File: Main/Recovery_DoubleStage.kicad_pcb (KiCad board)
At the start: 4 copper layers, 100.6 x 76.7 mm, 68 parts, among them IC1 ATMEGA2560-16AU, IC2 AP2210N-3.3TRG1, IC3 MMC5983MA, IC4 NEO-6M-0, IC5 BMP388, IC6 MPU-6050, J1 ICSP, J2 Conn_02x10_Counter_Clockwise, J3 Conn_Coaxial, J4 Conn_Coaxial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

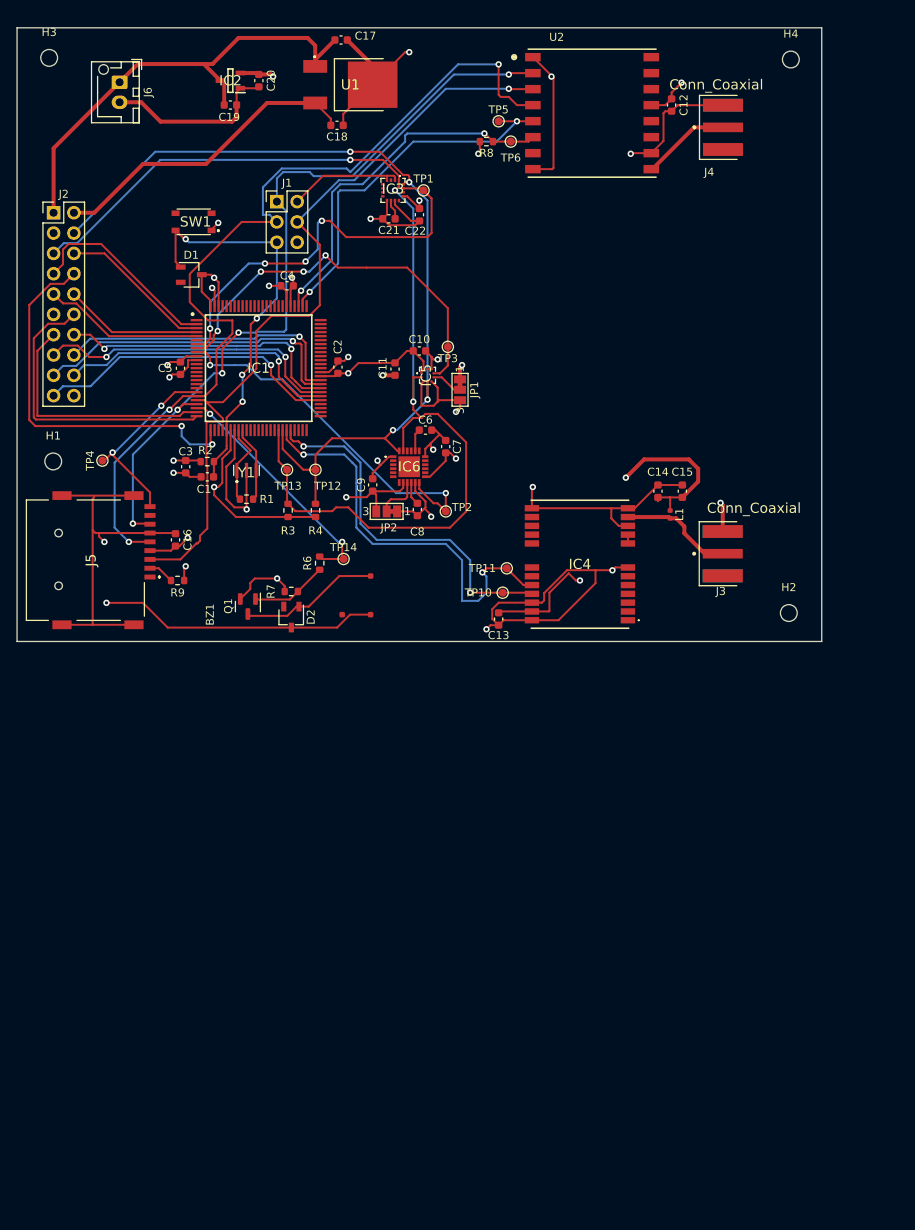
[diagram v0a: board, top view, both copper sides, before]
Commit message: added relative paths
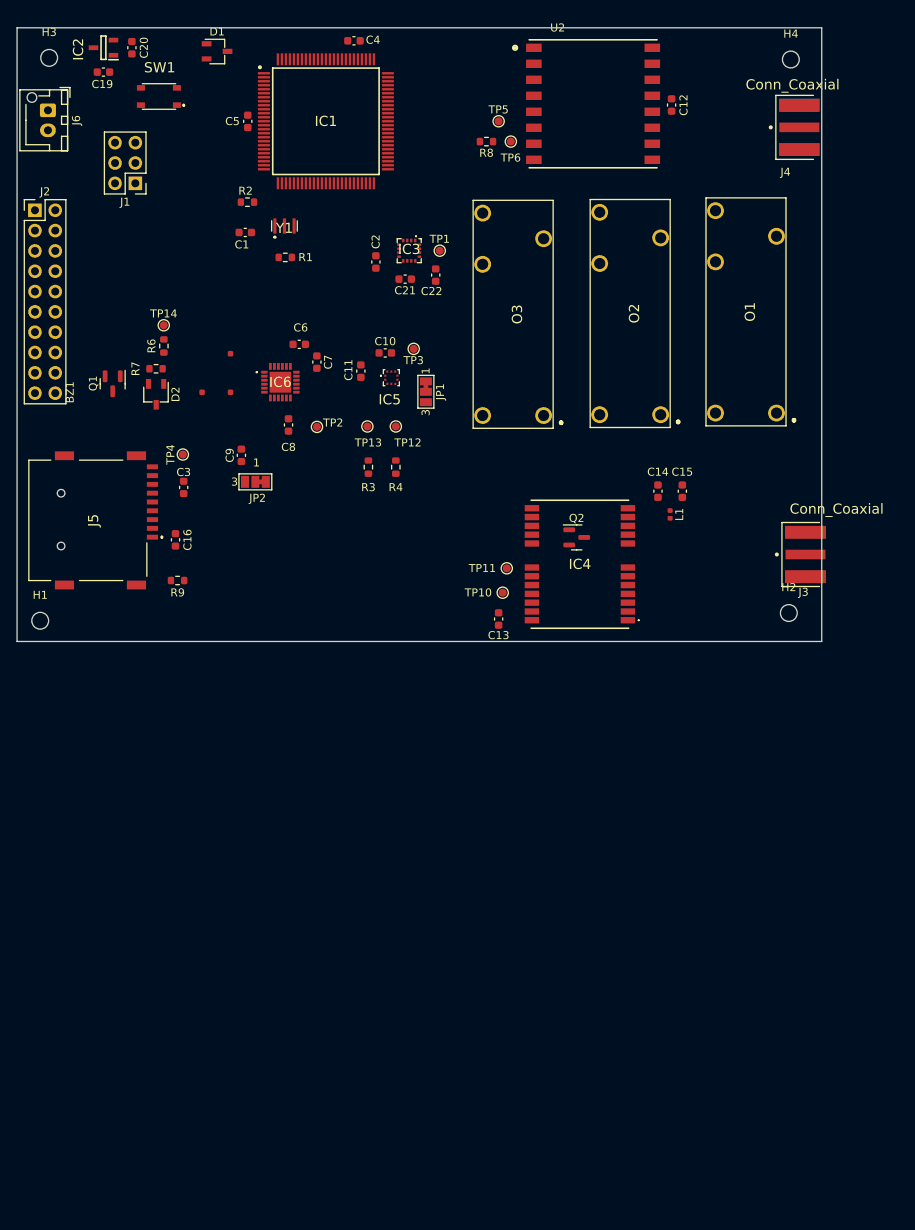
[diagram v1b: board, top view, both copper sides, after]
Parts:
- removed C17, C18: 10u, Capacitor_SMD:C_0603_1608Metric
- removed U1: NCP5501DT50RKG, Footprint:NCP5501DT50RKG
- added O1: G6RL-1-DC3, Footprint:G6RL1DC5, F.Cu at (107.4, 61.4)
- added O2: G6RL-1-DC3, Footprint:G6RL1DC5, F.Cu at (92.9, 61.6)
- added O3: G6RL-1-DC3, Footprint:G6RL1DC5, F.Cu at (78.3, 61.7)
- added Q2: BSS138, Package_TO_SOT_SMD:SOT-23, F.Cu at (82.4, 76.9)
- moved TP14 36.9 mm to (30.8, 50.4)
- moved R6 33.4 mm to (30.8, 53.0)
- moved BZ1 32.8 mm to (39.4, 58.8)
- moved R2 32.8 mm to (41.2, 35.0)
- moved Q1 32.6 mm to (24.4, 57.7)
- moved D2 32.6 mm to (29.8, 59.0)
- moved R7 32.6 mm to (29.8, 55.8)
- moved IC1 32.0 mm to (51.1, 24.9)
- moved C5 32.0 mm to (41.3, 24.9)
- moved C4 31.7 mm to (54.6, 14.8)
- moved C1 30.9 mm to (41.0, 38.8)
- moved Y1 30.9 mm to (45.9, 38.4)
- moved R1 30.6 mm to (46.0, 41.9)
- moved D1 28.1 mm to (37.5, 16.2)
- moved H1 20.0 mm to (15.3, 87.3)
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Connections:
- J2 pad 14: /IGNITION -> unconnected-(J2-Pad14)
- J2 pad 15: /ID3 -> unconnected-(J2-Pad15)
- J2 pad 16: /Relay_2 -> unconnected-(J2-Pad16)
- J2 pad 17: /Relay_1 -> unconnected-(J2-Pad17)
- J2 pad 18: /ID2 -> unconnected-(J2-Pad18)
- J2 pad 19: /ID1 -> unconnected-(J2-Pad19)
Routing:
- net GND: track 288.5 -> 0.00 mm, vias 23 -> 0
- net +3V3: track 188.2 -> 0.00 mm, vias 17 -> 0
- net /SCL: track 140.6 -> 0.00 mm, vias 3 -> 0
- net +5V: track 125.7 -> 0.00 mm, vias 1 -> 0
- net /SCK: track 112.7 -> 0.00 mm, vias 3 -> 0
- net /SDA: track 112.4 -> 0.00 mm, vias 4 -> 0
- net /MOSI: track 99.1 -> 0.00 mm, vias 1 -> 0
- net /MISO: track 98.2 -> 0.00 mm, vias 5 -> 0
- net +BATT: track 58.5 -> 0.00 mm
- net /RX1: track 52.4 -> 0.00 mm, vias 2 -> 0
- net /microcontroller/RESET: track 50.8 -> 0.00 mm, vias 4 -> 0
- net /BMP_INT: track 49.9 -> 0.00 mm, vias 4 -> 0
- net /MMC_INT: track 49.8 -> 0.00 mm, vias 4 -> 0
- net /OPT1: track 48.3 -> 0.00 mm, vias 2 -> 0
- net /MPU_INT: track 46.6 -> 0.00 mm, vias 2 -> 0
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- removed copper zone on In2.Cu, net +3V3
- removed copper zone on In1.Cu, net GND

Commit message: reviewed design. starting routing
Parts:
- removed C19, C20: 10u, Capacitor_SMD:C_0603_1608Metric
- removed IC2: AP2210N-3.3TRG1, Footprint:SOT95P280X145-3N
- added C17: 4.7u, Capacitor_SMD:C_0603_1608Metric, F.Cu at (21.1, 16.9)
- added C18: 10u, Capacitor_SMD:C_0603_1608Metric, F.Cu at (25.1, 20.2)
- added D3: D, Package_TO_SOT_SMD:TSOT-23, F.Cu at (62.5, 143.6)
- added D4: D, Package_TO_SOT_SMD:TSOT-23, F.Cu at (57.1, 143.6)
- added D5: D, Package_TO_SOT_SMD:TSOT-23, F.Cu at (67.9, 143.6)
- added IC7: PS2801C-4-F3-A, Footprint:SOIC127P700X230-16N, F.Cu at (41.2, 147.4)
- added J7: Screw_Terminal_01x06, TerminalBlock:TerminalBlock_bornier-6_P5.08mm, F.Cu at (39.7, 122.7)
- added J8: JSTXH-1x02, Connector_JST:JST_XH_B2B-XH-AM_1x02_P2.50mm_Vertical, F.Cu at (66.4, 131.1)
- added L2: 1uH, Inductor_SMD:L_0805_2012Metric, F.Cu at (27.9, 17.2)
- added Q3: BSS138, Package_TO_SOT_SMD:SOT-23, F.Cu at (73.0, 142.3)
- added Q4: BSS138, Package_TO_SOT_SMD:SOT-23, F.Cu at (77.9, 142.3)
- added R10: 100k, Resistor_SMD:R_0603_1608Metric, F.Cu at (60.4, 149.6)
- added R11: 100k, Resistor_SMD:R_0603_1608Metric, F.Cu at (48.0, 152.8)
- added R12: 1k, Resistor_SMD:R_0603_1608Metric, F.Cu at (64.0, 152.1)
- added R13: 1k, Resistor_SMD:R_0603_1608Metric, F.Cu at (56.0, 152.8)
- added R14: 1k, Resistor_SMD:R_0603_1608Metric, F.Cu at (64.5, 149.6)
- added R15: 100, Resistor_SMD:R_0603_1608Metric, F.Cu at (52.0, 152.8)
- added R16: 10k, Resistor_SMD:R_0603_1608Metric, F.Cu at (79.4, 133.6)
- added R17: 100, Resistor_SMD:R_0603_1608Metric, F.Cu at (68.0, 152.1)
- added R18: 10k, Resistor_SMD:R_0603_1608Metric, F.Cu at (68.5, 149.6)
- added R19: 100, Resistor_SMD:R_0603_1608Metric, F.Cu at (60.0, 152.1)
- added R20: 100, Resistor_SMD:R_0603_1608Metric, F.Cu at (56.4, 149.6)
- added R21: 100, Resistor_SMD:R_0603_1608Metric, F.Cu at (64.0, 147.1)
- added R22: 100, Resistor_SMD:R_0603_1608Metric, F.Cu at (72.0, 147.1)
- added R23: 10k, Resistor_SMD:R_0603_1608Metric, F.Cu at (60.0, 147.1)
- added R24: 330k, Resistor_SMD:R_0603_1608Metric, F.Cu at (107.9, 125.7)
- added R25: 100k, Resistor_SMD:R_0603_1608Metric, F.Cu at (70.7, 25.1)
- added R26: 330, Resistor_SMD:R_0603_1608Metric, F.Cu at (116.7, 119.4)
- added R27: 330, Resistor_SMD:R_0603_1608Metric, F.Cu at (111.9, 125.7)
- added R28: 330, Resistor_SMD:R_0603_1608Metric, F.Cu at (116.7, 121.9)
- added R5: 100k, Resistor_SMD:R_0603_1608Metric, F.Cu at (68.0, 147.1)
- added SW1: SW_Push, Footprint:PTS815SJK250SMTRLFS, F.Cu at (110.5, 121.3)
- added TP7: TestPoint, TestPoint:TestPoint_Pad_D1.0mm, F.Cu at (53.8, 160.8)
- added U1: Opamp_Quad, Attiny414:SOIC127P600X175-14N, F.Cu at (50.2, 146.5)
- added U3: ADP2108AUJ-3.3, Package_TO_SOT_SMD:TSOT-23-5, F.Cu at (24.0, 17.3)
- C1: value 22p -> 100nF
- H1, H2, H3, H4: footprint MountingHole:MountingHole_2.1mm -> MountingHole:MountingHole_3.2mm_M3
- moved L1 7.63 mm to (101.7, 73.1)
- moved TP11 7.61 mm to (81.2, 80.0)
- moved C14 7.61 mm to (100.1, 70.3)
- moved C15 7.61 mm to (103.2, 70.3)
- moved Q2 7.61 mm to (90.0, 76.1)
- moved C13 7.61 mm to (80.2, 86.3)
- moved IC4 7.61 mm to (90.4, 79.5)
- moved TP10 7.61 mm to (80.7, 83.0)
- moved J3 5.33 mm to (117.5, 73.8)
- moved SW1 3.42 mm to (33.6, 22.0)
- moved J4 3.32 mm to (117.8, 29.0)
- moved J5 2.54 mm to (21.6, 72.2)
- moved O3 1.68 mm to (79.6, 62.6)
- moved TP5 1.42 mm to (74.1, 24.9)
- moved O2 1.33 mm to (93.5, 62.7)
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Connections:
- net /ANT_LORA renamed Net-(J4-Pad1)
- IC1 pad 76: unconnected-(IC1-Pad76) -> /LoRa_Ready
- IC6 pad 25: unconnected-(IC6-Pad25) -> (no net)
- O1 pad 1: Net-(O1-Pad1) -> +3V3
- O1 pad 2: unconnected-(O1-Pad2) -> /igniter/igniter1-out
- O1 pad 3: unconnected-(O1-Pad3) -> +9V
- O1 pad 4: unconnected-(O1-Pad4) -> +9V
- O1 pad 5: Net-(O1-Pad5) -> Net-(D3-Pad2)
- O2 pad 1: unconnected-(O2-Pad1) -> +3V3
- O2 pad 2: unconnected-(O2-Pad2) -> /igniter/igniter2-out
- O2 pad 3: unconnected-(O2-Pad3) -> +9V
- O2 pad 4: unconnected-(O2-Pad4) -> +9V
- O2 pad 5: unconnected-(O2-Pad5) -> Net-(D4-Pad2)
- O3 pad 1: unconnected-(O3-Pad1) -> +3V3
- O3 pad 2: unconnected-(O3-Pad2) -> /igniter/igniter3-out
- O3 pad 3: unconnected-(O3-Pad3) -> +9V
- O3 pad 4: unconnected-(O3-Pad4) -> +9V
- O3 pad 5: unconnected-(O3-Pad5) -> Net-(D5-Pad2)
- Q2 pad 1: unconnected-(Q2-Pad1) -> Net-(Q2-Pad1)
- Q2 pad 2: unconnected-(Q2-Pad2) -> GND
- Q2 pad 3: unconnected-(Q2-Pad3) -> Net-(D3-Pad2)
- U2 pad 14: unconnected-(U2-Pad14) -> /LoRa_Ready

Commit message: finalized pcb
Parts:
- removed R9: 10k, Resistor_SMD:R_0603_1608Metric
- removed the SW1 at (33.6, 22.0)
- removed TP12: SDA, TestPoint:TestPoint_Pad_D1.0mm
- removed TP13: SCL, TestPoint:TestPoint_Pad_D1.0mm
- added C19: C_Polarized, Capacitor_SMD:CP_Elec_6.3x7.7, F.Cu at (61.5, 45.4)
- added G***: LOGO, Footprint:full_logo_21.3mmx9.3mm, F.Cu at (72.6, 84.6)
- added R29: 100k, Resistor_SMD:R_0603_1608Metric, B.Cu at (42.5, 71.7)
- added R30: 100k, Resistor_SMD:R_0603_1608Metric, B.Cu at (27.5, 84.8)
- added R31: 100k, Resistor_SMD:R_0603_1608Metric, B.Cu at (27.5, 70.7)
- added R32: 100, Resistor_SMD:R_0603_1608Metric, B.Cu at (45.1, 63.2)
- C10, C11, C21, C4, C5, IC1, IC3, IC4, IC5, IC7, J3, J4, JP1, L1, R1, R10, R11, R12, R14, R19, R20, R22, U2, Y1: moved to B.Cu
- R13: value 1k -> 100k; moved to B.Cu
- R5: value 100k -> 1k; moved to B.Cu
- U1: value Opamp_Quad -> LM339; footprint Attiny414:SOIC127P600X175-14N -> Package_SO:TSSOP-14_4.4x5mm_P0.65mm; moved to B.Cu
- moved TP7 130.1 mm to (82.5, 33.9)
- moved SW1 125.8 mm to (24.2, 29.8), turned to -90 degrees
- moved R24 121.8 mm to (26.9, 34.8)
- moved R28 115.1 mm to (43.1, 33.4), turned to 90 degrees
- moved R27 113.9 mm to (41.0, 36.6), turned to 90 degrees
- moved R26 111.9 mm to (45.2, 33.3), turned to 90 degrees
- moved R19 104.6 mm to (34.4, 50.7), turned to 90 degrees
- moved J8 104.4 mm to (17.0, 39.1), turned to -90 degrees
- moved R20 100.8 mm to (37.2, 50.6), turned to 90 degrees
- moved R22 100.3 mm to (42.3, 51.3)
- moved R11 98.5 mm to (27.6, 56.5)
- moved D5 95.5 mm to (55.2, 48.9)
- moved R23 94.7 mm to (53.8, 52.6), turned to 90 degrees
- moved R21 91.8 mm to (58.7, 55.4), turned to 180 degrees
- moved IC7 90.6 mm to (39.1, 56.8), turned to 90 degrees
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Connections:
- BZ1 pad 2: +5V -> +3V3
- C14 pad 2: +3V3 -> Net-(C14-Pad2)
- C15 pad 2: +3V3 -> Net-(C14-Pad2)
- D2 pad 3: +5V -> +3V3
- IC1 pad 20: /SCK -> /microcontroller/SCK_JTAG
- IC1 pad 21: /MOSI -> /microcontroller/MOSI_JTAG
- IC1 pad 22: /MISO -> /microcontroller/MISO_JTAG
- IC1 pad 58: /IGNITION -> /igniter/igniter1
- IC1 pad 59: /Relay_1 -> /igniter/igniter2
- IC1 pad 6: unconnected-(IC1-Pad6) -> /SD_CD
- IC1 pad 60: /Relay_2 -> /igniter/igniter3
- IC4 pad 8: Net-(IC4-Pad8) -> Net-(C14-Pad2)
- IC4 pad 9: Net-(IC4-Pad8) -> Net-(C14-Pad2)
- IC7 pad 1: /igniter/osense1_hv -> Net-(IC7-Pad1)
- IC7 pad 2: GND1 -> /igniter/osense1_hv
- IC7 pad 3: /igniter/osense2_hv -> Net-(IC7-Pad1)
- IC7 pad 4: GND1 -> /igniter/osense2_hv
- IC7 pad 5: /igniter/osense3_hv -> Net-(IC7-Pad1)
- IC7 pad 6: GND1 -> /igniter/osense3_hv
- J1 pad 1: /MISO -> /microcontroller/MISO_JTAG
- J1 pad 3: /SCK -> /microcontroller/SCK_JTAG
- J1 pad 4: /MOSI -> /microcontroller/MOSI_JTAG
- J2 pad 14: unconnected-(J2-Pad14) -> /SCK
- J2 pad 15: unconnected-(J2-Pad15) -> /MOSI
- J2 pad 16: unconnected-(J2-Pad16) -> /MISO
- J5 pad P2: Net-(J5-PadP2) -> /SD_CS
- J5 pad P9: /SD_CS -> /SD_CD
- L1 pad 1: +3V3 -> Net-(C14-Pad2)
- O1 pad 4: +9V -> /igniter/sense_1
- O2 pad 4: +9V -> /igniter/sense_2
- O3 pad 4: +9V -> /igniter/sense_3
- R11 pad 2: Net-(R11-Pad2) -> /igniter/sense_3
- R13 pad 1: Net-(R10-Pad2) -> +9V
- R13 pad 2: GND1 -> Net-(R12-Pad1)
- R14 pad 1: Net-(R11-Pad2) -> Net-(R14-Pad1)
- R16 pad 1: Net-(Q2-Pad1) -> GND
- R16 pad 2: Net-(D3-Pad2) -> Net-(Q2-Pad1)
- R18 pad 1: Net-(Q3-Pad1) -> GND
- R18 pad 2: Net-(D4-Pad2) -> Net-(Q3-Pad1)
- R23 pad 1: Net-(Q4-Pad1) -> GND
- R23 pad 2: Net-(D5-Pad2) -> Net-(Q4-Pad1)
- R26 pad 1: /MISO -> /microcontroller/MISO_JTAG
- R27 pad 1: /MOSI -> /microcontroller/MOSI_JTAG
- R28 pad 1: /SCK -> /microcontroller/SCK_JTAG
- R5 pad 1: +9V -> Net-(R10-Pad2)
- R5 pad 2: Net-(R12-Pad1) -> GND1
- U1 pad 1: /igniter/osense1_hv -> /igniter/osense2_hv
- U1 pad 10: +9V -> /igniter/sense_3
- U1 pad 11: GND1 -> Net-(R10-Pad2)
- U1 pad 12: (no net) -> GND1
- U1 pad 13: (no net) -> /igniter/osense3_hv
- U1 pad 2: Net-(R10-Pad2) -> /igniter/osense1_hv
- U1 pad 4: +9V -> /igniter/sense_1
- U1 pad 5: +9V -> Net-(R12-Pad1)
- U1 pad 6: Net-(R11-Pad2) -> /igniter/sense_2
- U1 pad 7: /igniter/osense2_hv -> Net-(R14-Pad1)
- U1 pad 8: /igniter/osense3_hv -> (no net)
- U1 pad 9: Net-(R12-Pad1) -> (no net)
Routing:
- net +3V3: track 0.00 -> 385.1 mm, vias 0 -> 15
- net GND: track 0.00 -> 313.4 mm, vias 0 -> 21
- net +9V: track 0.00 -> 155.2 mm, vias 0 -> 2
- net /igniter/igniter3: track 0.00 -> 150.1 mm, vias 0 -> 1
- net /igniter/igniter2: track 0.00 -> 128.5 mm, vias 0 -> 1
- net /igniter/igniter1: track 0.00 -> 109.9 mm, vias 0 -> 1
- net /SDA: track 0.00 -> 109.2 mm, vias 0 -> 5
- net /SCL: track 0.00 -> 105.4 mm, vias 0 -> 6
- net /TX1: track 0.00 -> 77.9 mm, vias 0 -> 1
- net /RX1: track 0.00 -> 77.1 mm, vias 0 -> 3
- net GND1: track 0.00 -> 76.1 mm, vias 0 -> 2
- net +BATT: track 0.00 -> 66.8 mm
- net /LoRa_Ready: track 0.00 -> 63.8 mm, vias 0 -> 3
- net /Buzzer: track 0.00 -> 60.0 mm, vias 0 -> 1
- net /BMP_INT: track 0.00 -> 55.1 mm, vias 0 -> 1
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- added copper zone on In1.Cu, net GND
- added copper zone on In2.Cu, net GND
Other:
- board size 100.6 x 76.7 mm -> 79 x 76.7 mm
- board text added: "9V"
- board text added: "designed by mac millan. Rev 2"
